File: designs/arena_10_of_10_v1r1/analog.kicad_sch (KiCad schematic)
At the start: 12 parts

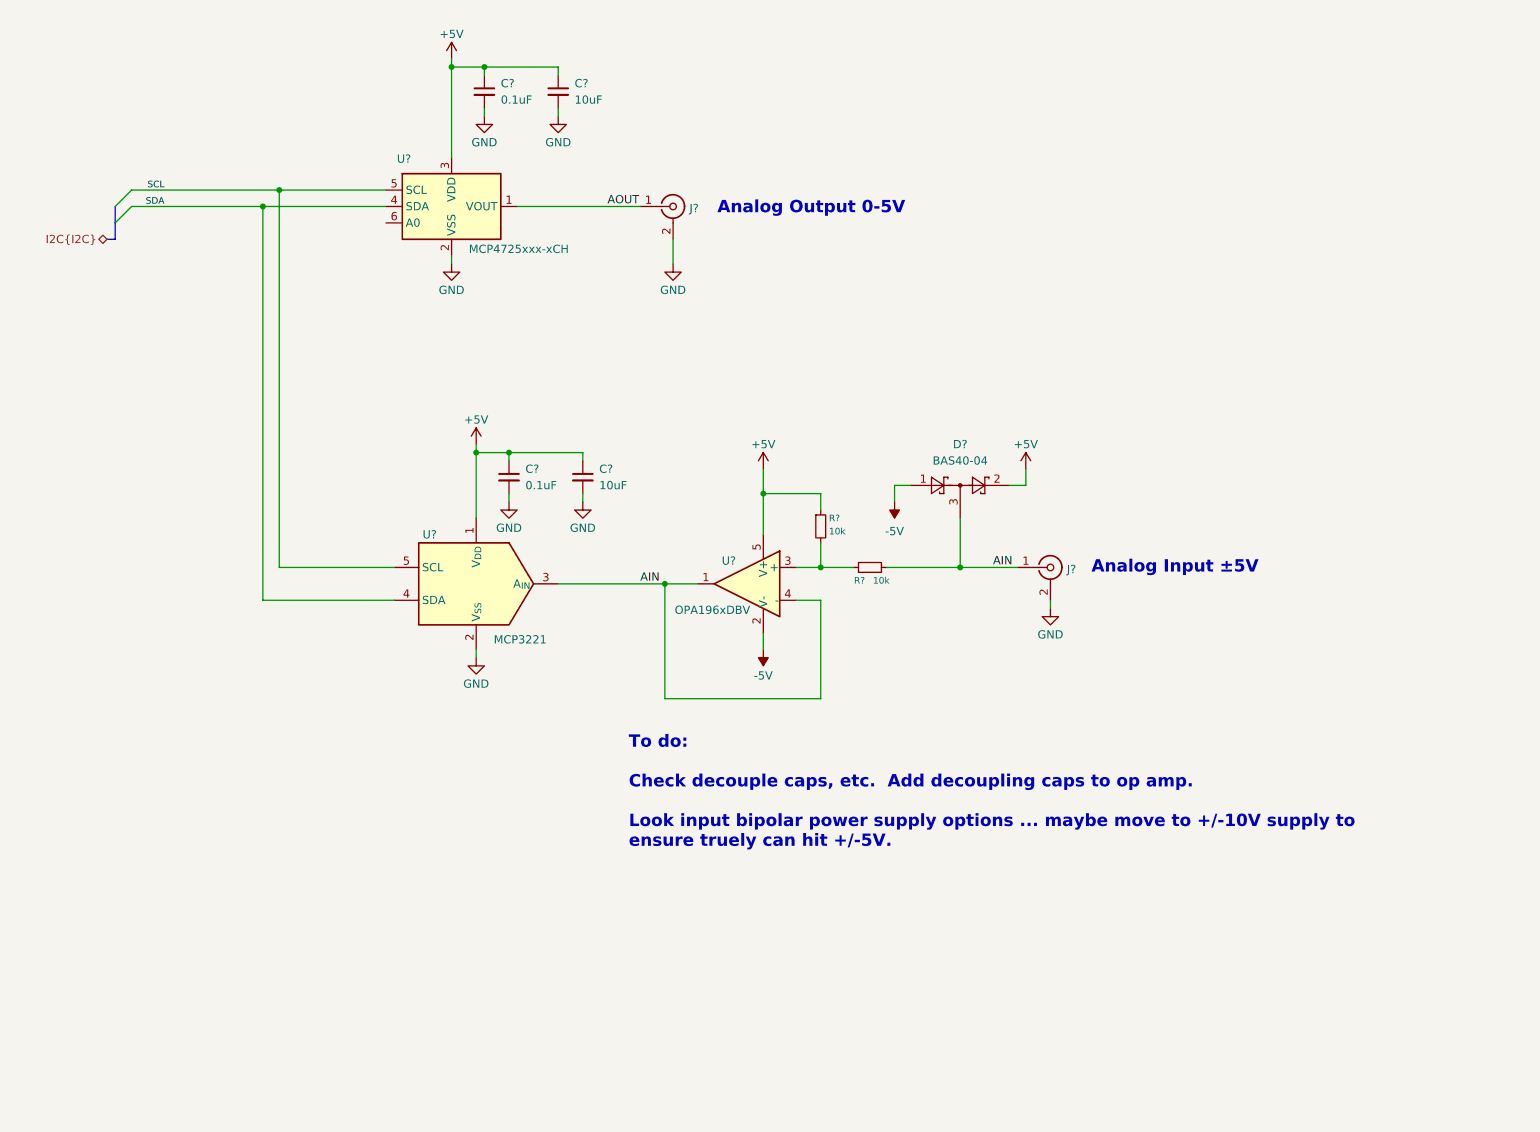
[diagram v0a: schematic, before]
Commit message: Re-worked MISO handling and analog input circuit.
Modified so that MISO isolation circuits are in fan out section and
are such that they will be placed close to the teensy.  Modified the
analog input circuit so that the teensy MCU analog inputs are used in
conjuction with a level shifting circuit.
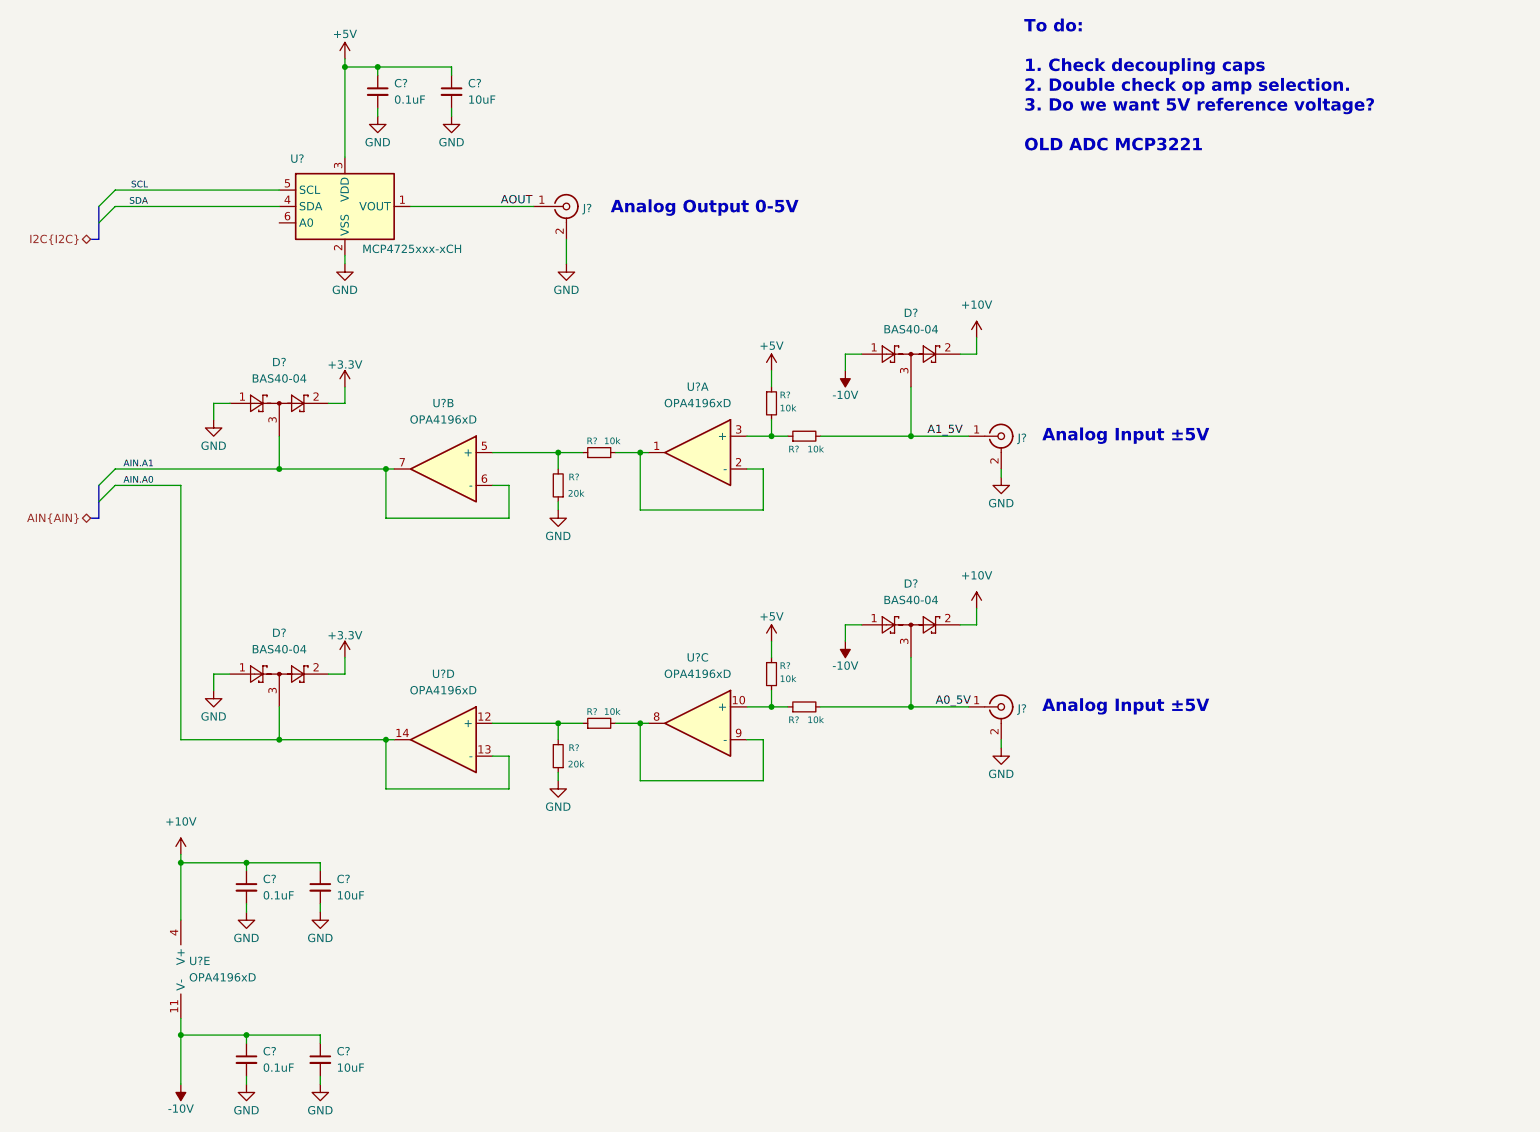
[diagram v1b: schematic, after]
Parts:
- removed C?: 10uF, symbol Device:C_Small
- removed C?: 0.1uF, symbol Device:C_Small
- removed U?: OPA196xDBV, Package_TO_SOT_SMD:SOT-23-5, symbol Amplifier_Operational:OPA196xDBV
- removed U?: MCP3221, Package_TO_SOT_SMD:SOT-23-5, symbol Analog_ADC:MCP3221
- added C? (x2): 10uF, symbol Device:C_Small
- added C? (x2): 0.1uF, symbol Device:C_Small
- added D? (x3): BAS40-04, Package_TO_SOT_SMD:SOT-23, symbol Diode:BAS40-04
- added J?: Conn_Coaxial, symbol Connector:Conn_Coaxial
- added R? (x2): 20k, symbol Device:R_Small
- added R? (x4): 10k, symbol Device:R_Small
- added U? (x5): OPA4196xD, Package_SO:SOIC-14_3.9x8.7mm_P1.27mm, symbol Amplifier_Operational:OPA4196xD
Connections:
- net +5V: now also R?.1; no longer D?.2
- net GND: now also C?.2, C?.2, C?.2, C?.2, D?.1, D?.1, J?.2 (Ext), R?.1, R?.1
- net at R?.1, R?.2: now also U?.3 (+)
- net -5V renamed -10V
- net -10V: now also C?.1, C?.1, D?.1, U?.11 (V-)
- net AIN renamed A1_5V
- new net: R?.1, R?.2, U?.12 (+)
- new net: R?.1, R?.2, U?.10 (+)
- new net: R?.1, R?.2, U?.5 (+)
- new net: R?.2, U?.8, U?.9 (-)
- new net: R?.2, U?.1, U?.2 (-)
- new net +10V: C?.1, C?.1, D?.2, D?.2, U?.4 (V+)
- new net +3.3V: D?.2, D?.2
- new net A0_5V: D?.3, J?.1 (In), R?.2
- new net AIN.A0: D?.3, U?.13 (-), U?.14
- new net AIN.A1: D?.3, U?.6 (-), U?.7
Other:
- note added: "To do: 1. Check decoupling caps 2. Double check op amp selection. 3. Do we want 5V reference voltage? OLD ADC MCP3221"
- note removed: "To do: Check decouple caps, etc. Add decoupling caps to op amp. Look input bipolar power supply options ... maybe move to +/-10V supply to ensure truely can hit +/-5V."
- moved on the sheet: C?, D?, J?, R?, U?
